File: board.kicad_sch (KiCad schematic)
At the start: 40 parts, among them P1 USB_C_Plug_USB2.0, Q1 BC847, Q2 BC847, SW1 SW_RST, SW2 SW_RST, U1 ESP32-WROOM-32(8MB), U3 CP2104

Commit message: feat: added relays and reworked programming
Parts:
- removed J3: (no value), Connector_PinHeader_2.54mm:PinHeader_1x04_P2.54mm_Vertical, symbol Connector:Conn_01x04_Female
- removed J4: (no value), Button_Switch_SMD:SW_DIP_SPSTx01_Slide_6.7x4.1mm_W6.73mm_P2.54mm_LowProfile_JPin, symbol Connector:Conn_01x02_Male
- removed J6: (no value), Connector_PinHeader_2.54mm:PinHeader_2x03_P2.54mm_Vertical, symbol Connector_Generic:Conn_02x03_Top_Bottom
- added J3, J4: Screw_Terminal_01x03, TerminalBlock_Phoenix:TerminalBlock_Phoenix_PT-1,5-3-5.0-H_1x03_P5.00mm_Horizontal, symbol Connector:Screw_Terminal_01x03
- added J6: Conn_01x05_Female, Connector_PinHeader_2.54mm:PinHeader_1x05_P2.54mm_Vertical_SMD_Pin1Left, symbol Connector:Conn_01x05_Female
- added K2, K3: SRD-05VDC-SL-C, SRD-05VDC-SL-C:RELAY_SRD-05VDC-SL-C, symbol SRD-05VDC-SL-C:SRD-05VDC-SL-C
- added Q3, Q4: BS170, Package_TO_SOT_THT:TO-92_Inline, symbol Transistor_FET:BS170
- added R14, R15, R16, R17: R, Resistor_SMD:R_0805_2012Metric, symbol Device:R
- C1, C2: value (none) -> 10uF
- C4: value (none) -> 100nF
- D1: value (none) -> SLED1
- D2: value (none) -> PLED
- D3: value (none) -> SLED2
- J1: value (none) -> TEMPS
- J2: value (none) -> OLED
- J5: value (none) -> PWR_IN
- R1: value (none) -> 4k7
- R2: value 1k -> 1k2
- R3: value (none) -> 10K
- R4, R5: value (none) -> 1k2
- U2: value (none) -> AMS1117-3.3
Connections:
- net +3V3: now also J6.1 (Pin_1)
- net CH1: now also Q3.2 (G), R14.2
- net CH2: now also Q4.2 (G), R15.2
- net GND: now also J6.5 (Pin_5), Q3.3 (S), Q4.3 (S), R14.1, R15.1
- net GPIO0: now also J6.4 (Pin_4)
- net RX_ESP: now also J6.2 (Pin_2)
- net TX_ESP: now also J6.3 (Pin_3)
- net VBUS: now also K2.A2, K3.A2
- new net: Q4.1 (D), R17.1
- new net: K3.A1, R17.2
- new net: Q3.1 (D), R16.1
- new net: K2.A1, R16.2
- new net: J3.2 (Pin_2), K2.COM
- new net: J3.3 (Pin_3), K2.NC
- new net: J3.1 (Pin_1), K2.NO
- new net: J4.2 (Pin_2), K3.COM
- new net: J4.3 (Pin_3), K3.NC
- new net: J4.1 (Pin_1), K3.NO
- no-connect marks 13 -> 12
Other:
- note added: "TODO: USB footprint integrate relay (https://www.robotics.org.za/SRD-5VDC-SL-C) opto isolator EL3H7(B)(TA)-G review Schaltplan"
- note added: "https://tinyurl.com/2as8tpyp"
- moved on the sheet: C1, C2, C3, C4, C5, C6, C7, C8, D1, D2, D3, D4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

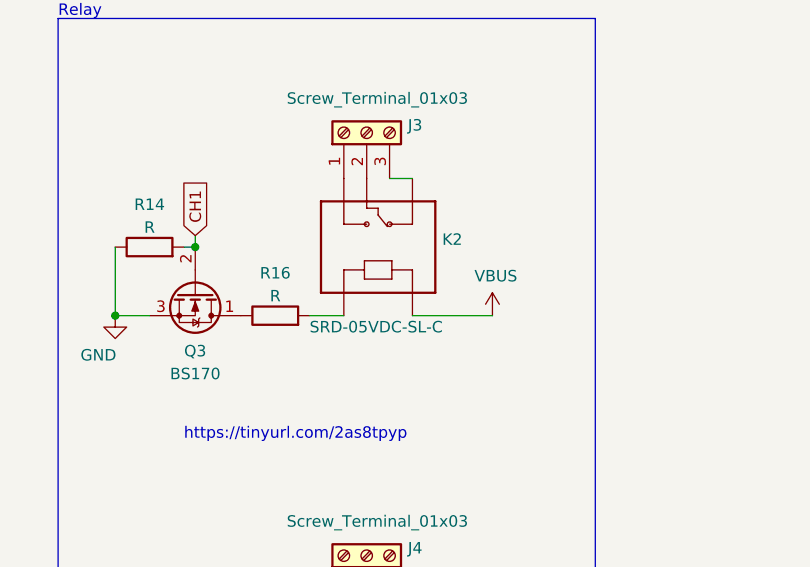
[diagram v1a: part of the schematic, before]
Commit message: feat: added relative pathing for relay libs
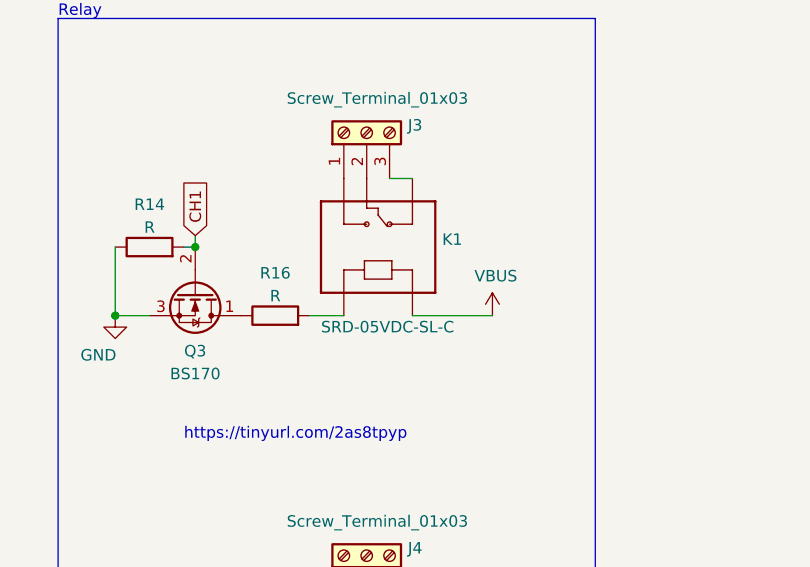
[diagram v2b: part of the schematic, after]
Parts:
- removed K2: SRD-05VDC-SL-C, SRD-05VDC-SL-C:RELAY_SRD-05VDC-SL-C, symbol SRD-05VDC-SL-C:SRD-05VDC-SL-C
- added K1: SRD-05VDC-SL-C, RELAY_SRD-05VDC-SL-C, symbol SRD-05VDC-SL-C:SRD-05VDC-SL-C
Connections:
- net VBUS: now also K1.A2
- net at R16.2: now also K1.A1
- net at J3.2 (Pin_2): now also K1.COM
- net at J3.3 (Pin_3): now also K1.NC
- net at J3.1 (Pin_1): now also K1.NO
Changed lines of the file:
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@@
     (pin "1")
-  )
-  (symbol (lib_id "SRD-05VDC-SL-C:SRD-05VDC-SL-C") (at 250.19 54.61 90) (unit 1)
-    (in_bom yes) (on_board yes)
-    (property "Reference" "K2" (id 0) (at 258.572 53.7753 90)
-      (effects (font (size 1.27 1.27)) (justify right))
-    )
-    (property "Value" "SRD-05VDC-SL-C" (id 1) (at 243.84 63.5 90)
-      (effects (font (size 1.27 1.27)) (justify right))
-    )
-    (property "Footprint" "SRD-05VDC-SL-C:RELAY_SRD-05VDC-SL-C" (id 2) (at 250.19 54.61 0)
-      (effects (font (size 1.27 1.27)) (justify left bottom) hide)
-    )
-    (property "Datasheet" "" (id 3) (at 250.19 54.61 0)
-      (effects (font (size 1.27 1.27)) (justify left bottom) hide)
-    )
-    (property "MANUFACTURER" "SONGLE RELAY" (id 4) (at 250.19 54.61 0)
-      (effects (font (size 1.27 1.27)) (justify left bottom) hide)
-    )
-    (property "STANDARD" "IPC-7251" (id 5) (at 250.19 54.61 0)
-      (effects (font (size 1.27 1.27)) (justify left bottom) hide)
-    )
-    (pin "A1")
-    (pin "A2")
-    (pin "COM")
-    (pin "NC")
-    (pin "NO")
   )
   (symbol (lib_id "Device:R") (at 114.3 83.82 0) (unit 1)
@@
     (pin "5")
   )
+  (symbol (lib_id "SRD-05VDC-SL-C:SRD-05VDC-SL-C") (at 250.19 54.61 90) (unit 1)
+    (in_bom yes) (on_board yes)
+    (property "Reference" "K1" (id 0) (at 258.572 53.7753 90)
+      (effects (font (size 1.27 1.27)) (justify right))
+    )
+    (property "Value" "SRD-05VDC-SL-C" (id 1) (at 245.11 63.5 90)
+      (effects (font (size 1.27 1.27)) (justify right))
+    )
+    (property "Footprint" "RELAY_SRD-05VDC-SL-C" (id 2) (at 250.19 54.61 0)
+      (effects (font (size 1.27 1.27)) (justify left bottom) hide)
+    )
+    (property "Datasheet" "" (id 3) (at 250.19 54.61 0)
+      (effects (font (size 1.27 1.27)) (justify left bottom) hide)
+    )
+    (property "MANUFACTURER" "SONGLE RELAY" (id 4) (at 250.19 54.61 0)
+      (effects (font (size 1.27 1.27)) (justify left bottom) hide)
+    )
+    (property "STANDARD" "IPC-7251" (id 5) (at 250.19 54.61 0)
+      (effects (font (size 1.27 1.27)) (justify left bottom) hide)
+    )
+    (pin "A1")
+    (pin "A2")
+    (pin "COM")
+    (pin "NC")
+    (pin "NO")
+  )
   (symbol (lib_id "Connector:Screw_Terminal_01x03") (at 250.19 41.91 90) (unit 1)
     (in_bom yes) (on_board yes)
@@
       (reference "J6") (unit 1) (value "Conn_01x05_Female") (footprint "Connector_PinHeader_2.54mm:PinHeader_1x05_P2.54mm_Vertical_SMD_Pin1Left")
     )
-    (path "/517987be-f4bc-463e-940e-559a1cddb50a"
-      (reference "K2") (unit 1) (value "SRD-05VDC-SL-C") (footprint "SRD-05VDC-SL-C:RELAY_SRD-05VDC-SL-C")
+    (path "/cd9e19f8-a56a-43d5-8b71-b7a9023174e6"
+      (reference "K1") (unit 1) (value "SRD-05VDC-SL-C") (footprint "RELAY_SRD-05VDC-SL-C")
     )
     (path "/8704f33b-8fd6-47c1-a736-e63be14f6f0c"

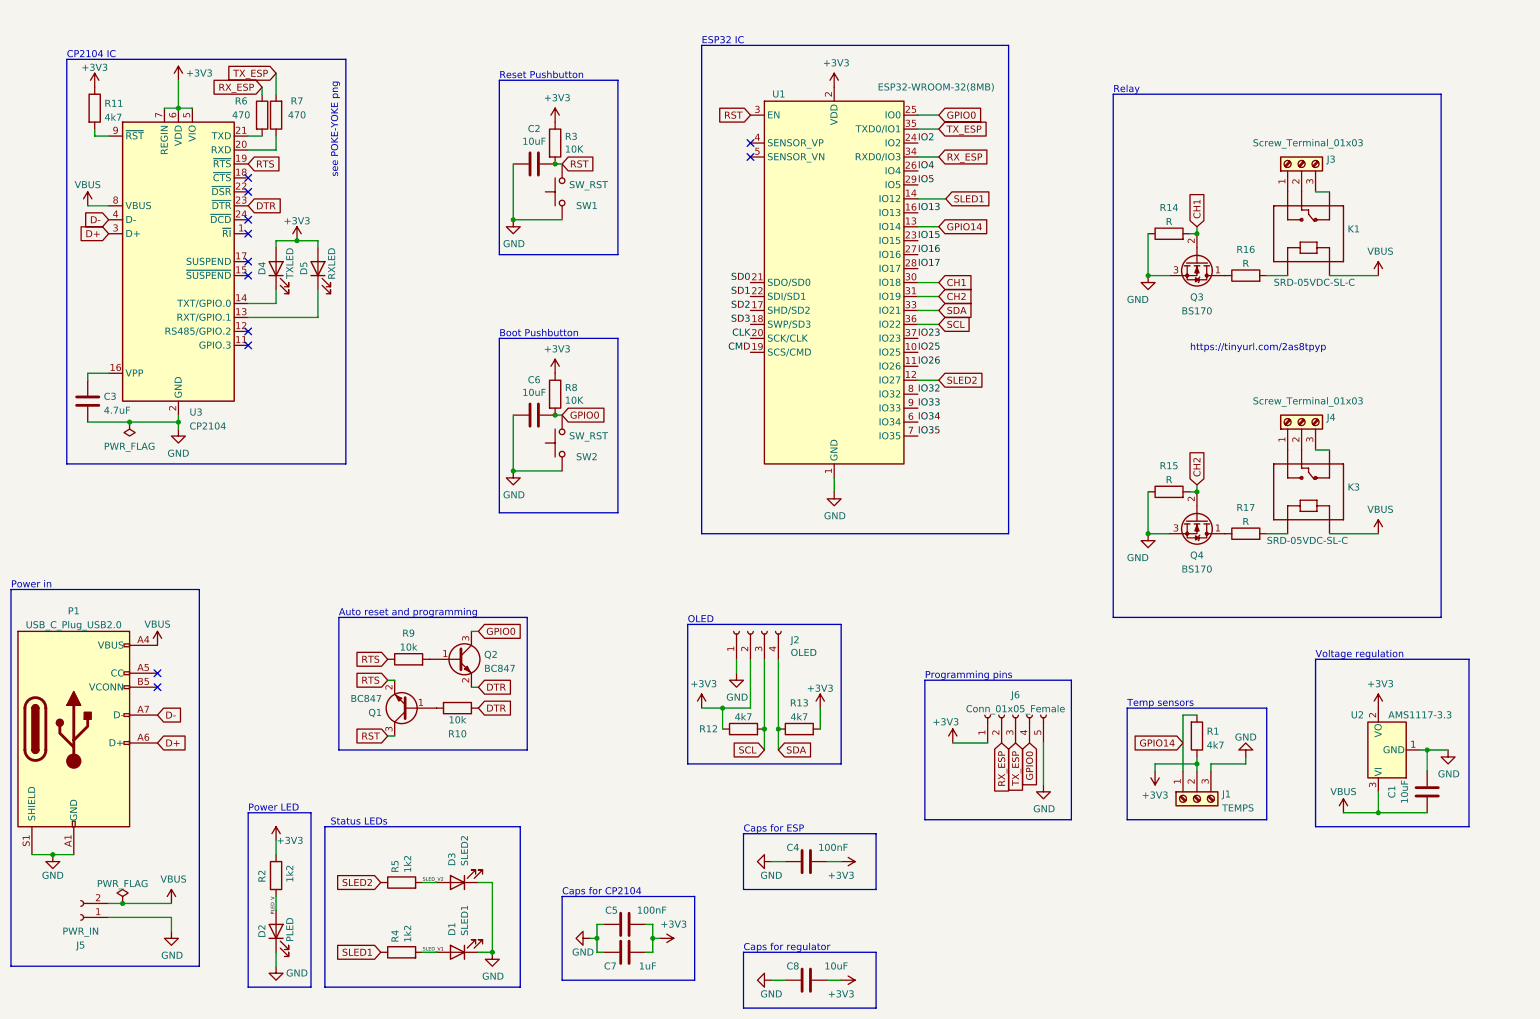
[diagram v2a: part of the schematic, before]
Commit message: feat: added usb-c connector and switched to ch340e
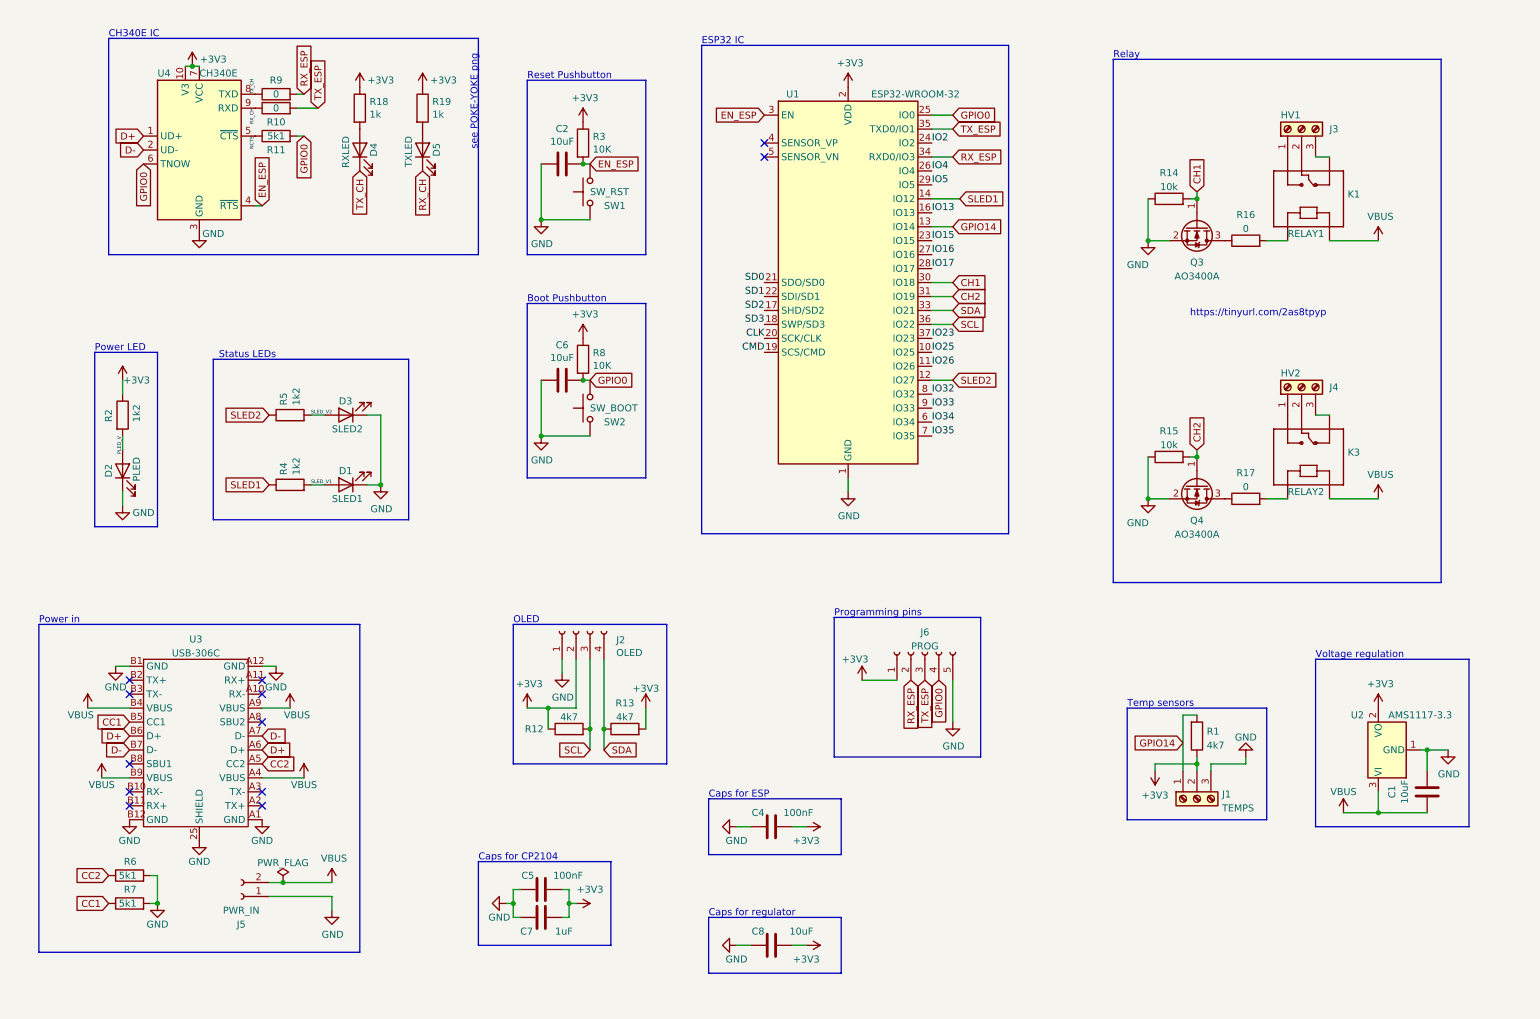
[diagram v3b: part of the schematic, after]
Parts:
- removed C3: 4.7uF, Capacitor_SMD:C_0805_2012Metric, symbol Device:C
- removed P1: USB_C_Plug_USB2.0, symbol Connector:USB_C_Plug_USB2.0
- removed Q1, Q2: BC847, Package_TO_SOT_SMD:SOT-23, symbol Transistor_BJT:BC847
- removed Q3, Q4: BS170, Package_TO_SOT_THT:TO-92_Inline, symbol Transistor_FET:BS170
- removed U3: CP2104, Package_DFN_QFN:QFN-24-1EP_4x4mm_P0.5mm_EP2.6x2.6mm, symbol Interface_USB:CP2104
- added Q3, Q4: AO3400A, Package_TO_SOT_SMD:SOT-23, symbol Transistor_FET:AO3400A
- added R18, R19: 1k, Resistor_SMD:R_0805_2012Metric, symbol Device:R
- added U3: USB-306C, board:USB-TYPE-C-TH_USB-306C, symbol board:USB-306C
- added U4: CH340E, Package_SO:MSOP-10_3x3mm_P0.5mm, symbol Interface_USB:CH340E
- D4: value TXLED -> RXLED
- D5: value RXLED -> TXLED
- J1: footprint Connector_PinHeader_2.54mm:PinHeader_1x03_P2.54mm_Vertical -> TerminalBlock_Phoenix:TerminalBlock_Phoenix_PT-1,5-3-5.0-H_1x03_P5.00mm_Horizontal
- J2: footprint Connector_PinHeader_2.54mm:PinHeader_1x04_P2.54mm_Vertical -> Connector_PinSocket_2.54mm:PinSocket_1x04_P2.54mm_Vertical
- J3: value Screw_Terminal_01x03 -> HV1
- J4: value Screw_Terminal_01x03 -> HV2
- J6: value Conn_01x05_Female -> PROG; footprint Connector_PinHeader_2.54mm:PinHeader_1x05_P2.54mm_Vertical_SMD_Pin1Left -> Connector_PinHeader_2.54mm:PinHeader_1x05_P2.54mm_Vertical
- K1: value SRD-05VDC-SL-C -> RELAY1; footprint RELAY_SRD-05VDC-SL-C -> SRD-05VDC-SL-C:RELAY_SRD-05VDC-SL-C
- K3: value SRD-05VDC-SL-C -> RELAY2
- R10, R9: value 10k -> 0
- R11: value 4k7 -> 5k1
- R14, R15: value R -> 10k
- R16, R17: value R -> 0
- R6, R7: value 470 -> 5k1
- SW1: footprint Button_Switch_THT:SW_PUSH_6mm_H13mm -> Button_Switch_THT:SW_PUSH_6mm_H4.3mm
- SW2: value SW_RST -> SW_BOOT; footprint Button_Switch_THT:SW_PUSH_6mm_H13mm -> Button_Switch_THT:SW_PUSH_6mm_H4.3mm
- U1: value ESP32-WROOM-32(8MB) -> ESP32-WROOM-32
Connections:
- net DTR is gone; now on net RX_CH: R10.1
- net RTS is gone; now on net TX_CH: R9.1
- net +3V3: now also R18.1, R19.1, U4.10 (V3), U4.7 (VCC); no longer D4.2 (A), D5.2 (A), R11.1
- net CH1: now also Q3.1 (G)
- net CH2: now also Q4.1 (G)
- net D+: now also U3.A6 (D+), U3.B6 (D+), U4.1 (UD+)
- net D-: now also U3.A7 (D-), U3.B7 (D-), U4.2 (UD-)
- net GND: now also R6.2, R7.2, Q3.2 (S), Q4.2 (S), U3.25 (SHIELD), U3.A1 (GND), U3.A12 (GND), U3.B1 (GND), U3.B12 (GND), U4.3 (GND)
- net GPIO0: now also R11.2, U4.6 (TNOW)
- net RX_ESP: now also R9.2; no longer R6.1
- net TX_ESP: now also R10.2; no longer R7.2
- net VBUS: now also U3.A4 (VBUS), U3.A9 (VBUS), U3.B4 (VBUS), U3.B9 (VBUS)
- net at R17.1: now also Q4.3 (D)
- net CC1: now reaches R7.1
- net CC1: now also U3.B5 (CC1)
- net at R16.1: now also Q3.3 (D)
- net RX_CH: now reaches D5.1 (K)
- net RX_CH: now also U4.9 (RXD)
- net TX_CH: now reaches D4.1 (K)
- net TX_CH: now also U4.8 (TXD)
- net RST renamed EN_ESP
- net EN_ESP: now also U4.4 (~{RTS})
- new net: D5.2 (A), R19.2
- new net: D4.2 (A), R18.2
- new net CC2: R6.1, U3.A5 (CC2)
- new net NCTS: R11.1, U4.5 (~{CTS})
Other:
- note added: "CH340E IC"
- note removed: "Auto reset and programming"
- note removed: "CP2104 IC"
- moved on the sheet: C2, C4, C5, C6, C7, C8, D1, D2, D3, J2, J3, J4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
